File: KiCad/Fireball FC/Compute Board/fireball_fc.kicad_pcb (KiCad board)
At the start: 4 copper layers, 36.3 x 31.8 mm, 37 parts, among them J1 Conn_01x04, J2 Conn_01x03, J4 Conn_01x09, J5 Conn_01x06, M1 MountingHole_2.2mm_M2, M2 MountingHole_2.2mm_M2, M3 MountingHole_2.2mm_M2, M4 MountingHole_2.2mm_M2, SW1 HX 3X4X2-2P-2.5N-04, U1 RP2040, U4 CAT24C256WI-GT3, U7 W25Q16JVUXIQ, X1 12MHZ Crystal

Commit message: finish compute, still needs cleanup
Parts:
- removed C21: 0.1uF, Capacitor_SMD:C_0402_1005Metric
- removed Card1: HYC77-TF09-200, lcsc_footprints:C341092_TF-SMD_HYC77-TF09-200
- removed R5: 220ohm, Resistor_SMD:R_0402_1005Metric
- added J3: Conn_01x04, Connector_PinHeader_2.00mm:PinHeader_1x04_P2.00mm_Vertical, F.Cu at (145.0, 91.4)
- C1, J1: moved to B.Cu
- C22: moved to F.Cu
- J5: value Conn_01x06 -> Conn_01x07; footprint Connector_PinHeader_2.00mm:PinHeader_1x06_P2.00mm_Vertical -> Connector_PinSocket_2.00mm:PinSocket_1x07_P2.00mm_Vertical
- moved C22 12.5 mm to (159.4, 73.8), turned to -90 degrees
- moved R3 3.13 mm to (155.5, 95.3), turned to 90 degrees
- moved J5 2.11 mm to (148.0, 94.6)
- moved C1 1.89 mm to (151.6, 86.4)
- moved R7 0.36 mm to (153.5, 67.9)
- moved J1 0.25 mm to (157.0, 89.5), turned to 90 degrees
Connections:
- U1 pad 17: /NEOPIXEL -> unconnected-(U1-GPIO14-Pad17)
- U1 pad 3: unconnected-(U1-GPIO1-Pad3) -> /5V_EN
- U1 pad 32: /5V_EN -> unconnected-(U1-GPIO21-Pad32)
- U1 pad 37: unconnected-(U1-GPIO25-Pad37) -> /NEOPIXEL
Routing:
- net +3V3: track 0.00 -> 27.8 mm, vias 6 -> 13
- net +5V: track 2.06 -> 29.0 mm, vias 3 -> 2
- net /USBDATA+: track 0.00 -> 25.2 mm, vias 0 -> 2
- net GND: track 0.98 -> 25.0 mm, vias 2 -> 24
- net /USBDATA-: track 0.00 -> 22.2 mm, vias 0 -> 2
- net /5V_EN: track 0.00 -> 21.2 mm, vias 0 -> 2
- net /~{QSPI_SS}: track 0.00 -> 15.6 mm
- net /GPS_TX: track 0.00 -> 15.1 mm, vias 0 -> 2
- net /GPS_RX: track 0.00 -> 13.9 mm, vias 0 -> 2
- net /NEOPIXEL: track 0.00 -> 13.6 mm
- net Net-(J1-Pin_3): track 0.00 -> 10.1 mm
- net Net-(J1-Pin_4): track 0.00 -> 8.62 mm
- net Net-(U1-DVDD-Pad23): track 0.00 -> 7.21 mm, vias 0 -> 2
- net /QSPI_SD2: track 0.00 -> 7.11 mm, vias 0 -> 2
- net /QSPI_SD1: track 0.00 -> 7.07 mm
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- added copper zone on F.Cu, net +3V3
- removed copper zone on In2.Cu, net +3V3
- removed copper zone on In1.Cu, net +5V
- removed copper zone on F.Cu, net GND
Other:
- board size 36.3 x 31.8 mm -> 36.7 x 32.1 mm
- copper layers 4 -> 2

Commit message: waow
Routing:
- net /~{QSPI_SS}: track 15.6 -> 14.7 mm

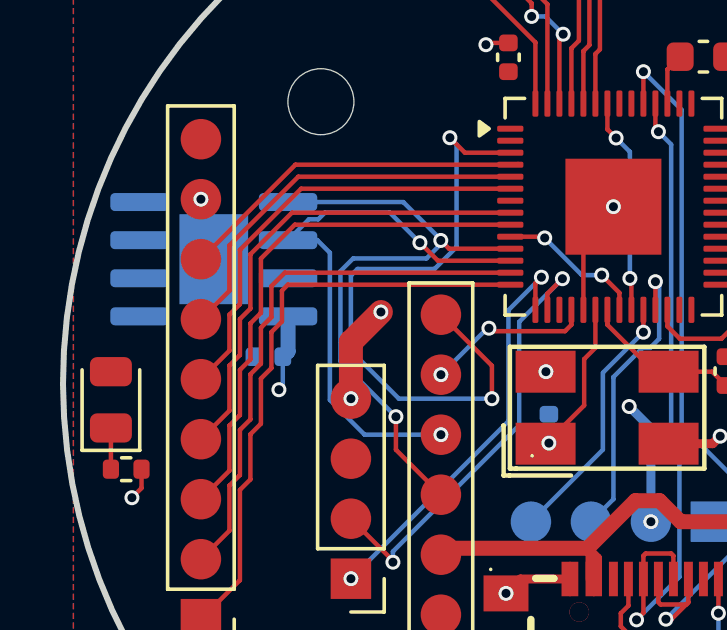
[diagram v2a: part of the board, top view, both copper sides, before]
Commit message: add 24LC512
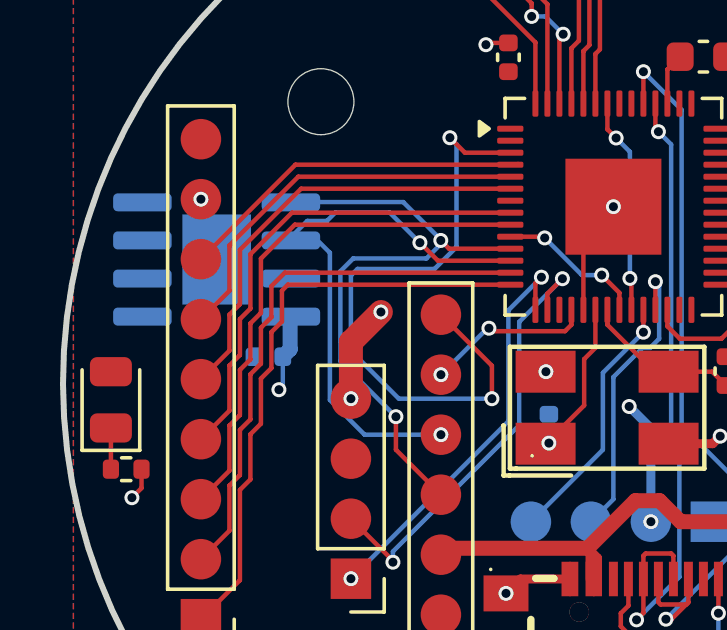
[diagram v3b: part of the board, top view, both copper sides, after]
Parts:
- removed U4: CAT24C256WI-GT3, Package_SO:SOIC-8-1EP_3.9x4.9mm_P1.27mm_EP2.29x3mm
- added U2: 24LC512, Package_SO:SOIC-8-1EP_3.9x4.9mm_P1.27mm_EP2.29x3mm, B.Cu at (140.5, 80.8)
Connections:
- U1 pad 27: /SDLED -> unconnected-(U1-GPIO16-Pad27)
- U1 pad 7: /SD_CS -> unconnected-(U1-GPIO5-Pad7)

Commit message: tweak traces
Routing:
- net GND: track 25.0 -> 28.2 mm, vias 24 -> 25
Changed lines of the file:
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@@
+	)
+	(segment
+		(start 148.5 78.85)
+		(end 148.95 78.4)
+		(width 0.15)
+		(layer "F.Cu")
+		(net "/SPI0_MISO")
 	)
 	(segment
 		(start 140.95 82.6)
+		(end 141.3 82.25)
+		(width 0.15)
+		(layer "F.Cu")
+		(net "/SPI0_MISO")
+	)
+	(segment
+		(start 141.3 82.25)
+		(end 141.3 80.439948)
+		(width 0.15)
+		(layer "F.Cu")
+		(net "/SPI0_MISO")
+	)
+	(segment
+		(start 140 84.75)
 		(end 140.95 83.8)
 		(width 0.15)
@@
 	)
 	(segment
+		(start 148.95 78.4)
+		(end 150.3125 78.4)
+		(width 0.15)
+		(layer "F.Cu")
+		(net "/SPI0_MISO")
+	)
+	(segment
 		(start 141.3 80.439948)
-		(end 141.3 82.25)
-		(width 0.15)
-		(layer "F.Cu")
-		(net "/SPI0_MISO")
-	)
-	(segment
-		(start 141.3 82.25)
+		(end 142.889948 78.85)
+		(width 0.15)
+		(layer "F.Cu")
+		(net "/SPI0_MISO")
+	)
+	(segment
+		(start 142.889948 78.85)
+		(end 148.5 78.85)
+		(width 0.15)
+		(layer "F.Cu")
+		(net "/SPI0_MISO")
+	)
+	(segment
+		(start 140.95 83.8)
 		(end 140.95 82.6)
-		(width 0.15)
-		(layer "F.Cu")
-		(net "/SPI0_MISO")
-	)
-	(segment
-		(start 140.95 83.8)
-		(end 140 84.75)
-		(width 0.15)
-		(layer "F.Cu")
-		(net "/SPI0_MISO")
-	)
-	(segment
-		(start 143.339948 78.4)
-		(end 141.3 80.439948)
-		(width 0.15)
-		(layer "F.Cu")
-		(net "/SPI0_MISO")
-	)
-	(segment
-		(start 150.3125 78.4)
-		(end 143.339948 78.4)
 		(width 0.15)
 		(layer "F.Cu")
@@
 	)
 	(segment
+		(start 148.855026 78)
+		(end 148.355026 78.5)
+		(width 0.15)
+		(layer "F.Cu")
+		(net "/SPI0_MOSI")
+	)
+	(segment
+		(start 148.355026 78.5)
+		(end 142.744973 78.5)
+		(width 0.15)
+		(layer "F.Cu")
+		(net "/SPI0_MOSI")
+	)
+	(segment
 		(start 150.3125 78)
-		(end 143.244974 78)
+		(end 148.855026 78)
+		(width 0.15)
+		(layer "F.Cu")
+		(net "/SPI0_MOSI")
+	)
+	(segment
+		(start 142.744973 78.5)
+		(end 140.95 80.294974)
 		(width 0.15)
 		(layer "F.Cu")
@@
 	)
 	(segment
-		(start 143.244974 78)
-		(end 140.95 80.294974)
-		(width 0.15)
-		(layer "F.Cu")
-		(net "/SPI0_MOSI")
-	)
-	(segment
 		(start 150.55 77.6)
 		(end 150.575 77.575)
@@
 	(segment
 		(start 150.3125 77.6)
-		(end 143.15 77.6)
+		(end 148.760052 77.6)
 		(width 0.15)
 		(layer "F.Cu")
@@
 	)
 	(segment
-		(start 143.15 77.6)
+		(start 148.210052 78.15)
+		(end 142.599999 78.15)
+		(width 0.15)
+		(layer "F.Cu")
+		(net "/SPI0_SCK")
+	)
+	(segment
+		(start 142.599999 78.15)
 		(end 140 80.75)
+		(width 0.15)
+		(layer "F.Cu")
+		(net "/SPI0_SCK")
+	)
+	(segment
+		(start 148.760052 77.6)
+		(end 148.210052 78.15)
 		(width 0.15)
 		(layer "F.Cu")
@@
 	)
 	(segment
+		(start 158.85 88.3)
+		(end 156.92 88.3)
+		(width 0.5)
+		(layer "F.Cu")
+		(net "GND")
+	)
+	(segment
 		(start 138.02 87.75)
 		(end 138.02 88.38)
@@
 	)
 	(via
+		(at 156.92 88.3)
+		(size 0.5)
+		(drill 0.3)
+		(layers "F.Cu" "B.Cu")
+		(free yes)
+		(net "GND")
+	)
+	(via
 		(at 150.17 91.89)
 		(size 0.5)
@@
 	)
 	(via
+		(at 158.85 88.3)
+		(size 0.5)
+		(drill 0.3)
+		(layers "F.Cu" "B.Cu")
+		(free yes)
+		(net "GND")
+	)
+	(via
 		(at 160.83 91.89)
 		(size 0.5)
@@
 	)
 	(via
-		(at 145 85.4)
-		(size 0.5)
-		(drill 0.3)
-		(layers "F.Cu" "B.Cu")
-		(net "GND")
-	)
-	(via
 		(at 168.835 83.8)
 		(size 0.5)
@@
 		(net "GND")
 	)
+	(segment
+		(start 157 89.5)
+		(end 157 88.38)
+		(width 0.5)
+		(layer "B.Cu")
+		(net "GND")
+	)
+	(segment
+		(start 157 88.38)
+		(end 156.92 88.3)
+		(width 0.5)
+		(layer "B.Cu")
+		(net "GND")
+	)

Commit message: update silkscreen
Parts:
- added G***: LOGO, LOGO, F.Cu at (162.8, 86.2)
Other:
- board text added: "@icechez"
- board text added: "@sjacksonhodum"
- board text added: "fireball"
- board text added: "v1"
